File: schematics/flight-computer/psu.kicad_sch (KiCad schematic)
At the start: 32 parts, among them Q1 Si9933CDY, Q2 BSS138, U10 LTC4002-ES8, U11 MAX604, U12 MAX604, U9 BQ29200

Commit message: Rename to Lychee
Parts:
- C31, C32, C33, C34, C35, C36, C37, C38, C39, C40, C41, C42: footprint Strix:C_0402 -> Lychee:C_0402
- D15, D16: footprint Strix:B330 -> Lychee:B330
- L8: footprint Strix:L_Wuerth_HCI-7050 -> Lychee:L_Wuerth_HCI-7050
- Q1: footprint Strix:Si9933CDY -> Lychee:Si9933CDY
- Q2: footprint Strix:BSS138 -> Lychee:BSS138
- R11, R12, R13, R14, R15, R16, R17, R18, R19, R20, R21: footprint Strix:R_0402 -> Lychee:R_0402
- U10: footprint Strix:LTC4002-ES8 -> Lychee:LTC4002-ES8
- U11, U12: footprint Strix:MAX604 -> Lychee:MAX604
- U9: footprint Strix:BQ29200 -> Lychee:BQ29200
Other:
- company: (none) -> Cambridge University Spaceflight
- title: (none) -> Lychee Flight Computer
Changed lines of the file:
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@@
 (kicad_sch (version 20211123) (generator eeschema)
   (paper "A4")
+  (title_block
+    (title "Lychee Flight Computer")
+    (date "2021-12-31")
+    (rev "1")
+    (company "Cambridge University Spaceflight")
+    (comment 1 "Drawn By H. Franks")
+  )
   (junction (at 45.72 171.45) (diameter 0) (color 0 0 0 0)
   )
@@
       (effects (font (size 1.27 1.27)) (justify left))
     )
-    (property "Footprint" "Strix:C_0402" (id 2) (at 115.57 161.29 0)
+    (property "Footprint" "Lychee:C_0402" (id 2) (at 115.57 161.29 0)
       (effects (font (size 1.27 1.27)) hide)
     )
@@
       (effects (font (size 1.27 1.27)) (justify left))
     )
-    (property "Footprint" "Strix:C_0402" (id 2) (at 102.87 62.23 0)
+    (property "Footprint" "Lychee:C_0402" (id 2) (at 102.87 62.23 0)
       (effects (font (size 1.27 1.27)) hide)
     )
@@
     (property "Reference" "R13" (id 0) (at 45.72 63.5 0))
     (property "Value" "261" (id 1) (at 45.72 66.04 0))
-    (property "Footprint" "Strix:R_0402" (id 2) (at 44.45 64.77 0)
+    (property "Footprint" "Lychee:R_0402" (id 2) (at 44.45 64.77 0)
       (effects (font (size 1.27 1.27)) hide)
     )
@@
       (effects (font (size 1.27 1.27)) (justify right))
     )
-    (property "Footprint" "Strix:LTC4002-ES8" (id 2) (at 83.82 120.65 0)
+    (property "Footprint" "Lychee:LTC4002-ES8" (id 2) (at 83.82 120.65 0)
       (effects (font (size 1.27 1.27)) hide)
     )
@@
     (property "Reference" "Q1" (id 0) (at 107.95 114.3 90))
     (property "Value" "Si9933CDY" (id 1) (at 107.95 116.84 90))
-    (property "Footprint" "Strix:Si9933CDY" (id 2) (at 106.045 118.11 0)
+    (property "Footprint" "Lychee:Si9933CDY" (id 2) (at 106.045 118.11 0)
       (effects (font (size 1.27 1.27) italic) (justify left) hide)
     )
@@
       (effects (font (size 1.27 1.27)) (justify left))
     )
-    (property "Footprint" "Strix:C_0402" (id 2) (at 245.11 58.42 0)
+    (property "Footprint" "Lychee:C_0402" (id 2) (at 245.11 58.42 0)
       (effects (font (size 1.27 1.27)) hide)
     )
@@
       (effects (font (size 1.27 1.27)) (justify left))
     )
-    (property "Footprint" "Strix:C_0402" (id 2) (at 50.8 67.31 0)
+    (property "Footprint" "Lychee:C_0402" (id 2) (at 50.8 67.31 0)
       (effects (font (size 1.27 1.27)) hide)
     )
@@
     (property "Reference" "R16" (id 0) (at 49.53 158.75 0))
     (property "Value" "100" (id 1) (at 49.53 161.29 0))
-    (property "Footprint" "Strix:R_0402" (id 2) (at 48.26 163.83 0)
+    (property "Footprint" "Lychee:R_0402" (id 2) (at 48.26 163.83 0)
       (effects (font (size 1.27 1.27)) hide)
     )
@@
       (effects (font (size 1.27 1.27)) (justify left))
     )
-    (property "Footprint" "Strix:R_0402" (id 2) (at 233.68 88.9 0)
+    (property "Footprint" "Lychee:R_0402" (id 2) (at 233.68 88.9 0)
       (effects (font (size 1.27 1.27)) hide)
     )
@@
       (effects (font (size 1.27 1.27)) (justify left))
     )
-    (property "Footprint" "Strix:L_Wuerth_HCI-7050" (id 2) (at 115.57 130.81 0)
+    (property "Footprint" "Lychee:L_Wuerth_HCI-7050" (id 2) (at 115.57 130.81 0)
       (effects (font (size 1.27 1.27)) hide)
     )
@@
     (property "Reference" "D15" (id 0) (at 50.8 102.87 0))
     (property "Value" "B330" (id 1) (at 50.8 105.41 0))
-    (property "Footprint" "Strix:B330" (id 2) (at 53.34 108.712 0)
+    (property "Footprint" "Lychee:B330" (id 2) (at 53.34 108.712 0)
       (effects (font (size 1.27 1.27)) hide)
     )
@@
       (effects (font (size 1.27 1.27)) (justify left))
     )
-    (property "Footprint" "Strix:C_0402" (id 2) (at 245.11 88.9 0)
+    (property "Footprint" "Lychee:C_0402" (id 2) (at 245.11 88.9 0)
       (effects (font (size 1.27 1.27)) hide)
     )
@@
       (effects (font (size 1.27 1.27)) (justify left))
     )
-    (property "Footprint" "Strix:C_0402" (id 2) (at 83.82 160.02 0)
+    (property "Footprint" "Lychee:C_0402" (id 2) (at 83.82 160.02 0)
       (effects (font (size 1.27 1.27)) hide)
     )
@@
       (effects (font (size 1.27 1.27)) (justify left))
     )
-    (property "Footprint" "Strix:C_0402" (id 2) (at 50.8 59.69 0)
+    (property "Footprint" "Lychee:C_0402" (id 2) (at 50.8 59.69 0)
       (effects (font (size 1.27 1.27)) hide)
     )
@@
       (effects (font (size 1.27 1.27)) (justify left))
     )
-    (property "Footprint" "Strix:C_0402" (id 2) (at 63.5 73.66 0)
+    (property "Footprint" "Lychee:C_0402" (id 2) (at 63.5 73.66 0)
       (effects (font (size 1.27 1.27)) hide)
     )
@@
     (property "Reference" "R14" (id 0) (at 45.72 71.12 0))
     (property "Value" "100" (id 1) (at 45.72 73.66 0))
-    (property "Footprint" "Strix:R_0402" (id 2) (at 44.45 72.39 0)
+    (property "Footprint" "Lychee:R_0402" (id 2) (at 44.45 72.39 0)
       (effects (font (size 1.27 1.27)) hide)
     )
@@
       (effects (font (size 1.27 1.27)) (justify left top))
     )
-    (property "Footprint" "Strix:C_0402" (id 2) (at 68.58 123.19 0)
+    (property "Footprint" "Lychee:C_0402" (id 2) (at 68.58 123.19 0)
       (effects (font (size 1.27 1.27)) hide)
     )
@@
       (effects (font (size 1.27 1.27)) (justify left))
     )
-    (property "Footprint" "Strix:R_0402" (id 2) (at 102.87 48.26 0)
+    (property "Footprint" "Lychee:R_0402" (id 2) (at 102.87 48.26 0)
       (effects (font (size 1.27 1.27)) hide)
     )
@@
       (effects (font (size 1.27 1.27)) (justify left))
     )
-    (property "Footprint" "Strix:R_0402" (id 2) (at 115.57 144.78 0)
+    (property "Footprint" "Lychee:R_0402" (id 2) (at 115.57 144.78 0)
       (effects (font (size 1.27 1.27)) hide)
     )
@@
       (effects (font (size 1.27 1.27)) (justify left))
     )
-    (property "Footprint" "Strix:C_0402" (id 2) (at 201.93 58.42 0)
+    (property "Footprint" "Lychee:C_0402" (id 2) (at 201.93 58.42 0)
       (effects (font (size 1.27 1.27)) hide)
     )
@@
       (effects (font (size 1.27 1.27)) (justify left))
     )
-    (property "Footprint" "Strix:BSS138" (id 2) (at 63.5 165.735 0)
+    (property "Footprint" "Lychee:BSS138" (id 2) (at 63.5 165.735 0)
       (effects (font (size 1.27 1.27) italic) (justify left) hide)
     )
@@
       (effects (font (size 1.27 1.27)) (justify left))
     )
-    (property "Footprint" "Strix:C_0402" (id 2) (at 100.33 123.19 0)
+    (property "Footprint" "Lychee:C_0402" (id 2) (at 100.33 123.19 0)
       (effects (font (size 1.27 1.27)) hide)
     )
@@
     (property "Reference" "R12" (id 0) (at 45.72 55.88 0))
     (property "Value" "160" (id 1) (at 45.72 58.42 0))
-    (property "Footprint" "Strix:R_0402" (id 2) (at 44.45 57.15 0)
+    (property "Footprint" "Lychee:R_0402" (id 2) (at 44.45 57.15 0)
       (effects (font (size 1.27 1.27)) hide)
     )
@@
     (property "Reference" "U11" (id 0) (at 220.98 45.9232 0))
     (property "Value" "MAX604" (id 1) (at 220.98 48.2346 0))
-    (property "Footprint" "Strix:MAX604" (id 2) (at 220.98 46.355 0)
+    (property "Footprint" "Lychee:MAX604" (id 2) (at 220.98 46.355 0)
       (effects (font (size 1.27 1.27) italic) hide)
     )
@@
       (effects (font (size 1.27 1.27)) (justify right))
     )
-    (property "Footprint" "Strix:R_0402" (id 2) (at 41.91 129.54 0)
+    (property "Footprint" "Lychee:R_0402" (id 2) (at 41.91 129.54 0)
       (effects (font (size 1.27 1.27)) hide)
     )
@@
     (property "Reference" "R21" (id 0) (at 240.03 83.82 0))
     (property "Value" "100k" (id 1) (at 240.03 86.36 0))
-    (property "Footprint" "Strix:R_0402" (id 2) (at 238.76 85.09 0)
+    (property "Footprint" "Lychee:R_0402" (id 2) (at 238.76 85.09 0)
       (effects (font (size 1.27 1.27)) hide)
     )
@@
       (effects (font (size 1.27 1.27)) (justify right))
     )
-    (property "Footprint" "Strix:B330" (id 2) (at 125.222 137.16 0)
+    (property "Footprint" "Lychee:B330" (id 2) (at 125.222 137.16 0)
       (effects (font (size 1.27 1.27)) hide)
     )
@@
       (effects (font (size 1.27 1.27)) (justify left))
     )
-    (property "Footprint" "Strix:C_0402" (id 2) (at 201.93 88.9 0)
+    (property "Footprint" "Lychee:C_0402" (id 2) (at 201.93 88.9 0)
       (effects (font (size 1.27 1.27)) hide)
     )
@@
     (property "Reference" "Q1" (id 0) (at 50.8 114.3 90))
     (property "Value" "Si9933CDY" (id 1) (at 50.8 116.84 90))
-    (property "Footprint" "Strix:Si9933CDY" (id 2) (at 52.705 118.11 0)
+    (property "Footprint" "Lychee:Si9933CDY" (id 2) (at 52.705 118.11 0)
       (effects (font (size 1.27 1.27) italic) (justify left) hide)
     )
@@
       (effects (font (size 1.27 1.27)) (justify left))
     )
-    (property "Footprint" "Strix:R_0402" (id 2) (at 45.72 166.37 0)
+    (property "Footprint" "Lychee:R_0402" (id 2) (at 45.72 166.37 0)
       (effects (font (size 1.27 1.27)) hide)
     )
@@
       (effects (font (size 1.27 1.27)) (justify right))
     )
-    (property "Footprint" "Strix:BQ29200" (id 2) (at 63.5 49.53 0)
+    (property "Footprint" "Lychee:BQ29200" (id 2) (at 63.5 49.53 0)
       (effects (font (size 1.27 1.27)) hide)
     )
@@
       (effects (font (size 1.27 1.27)) (justify left))
     )
-    (property "Footprint" "Strix:R_0402" (id 2) (at 83.82 166.37 0)
+    (property "Footprint" "Lychee:R_0402" (id 2) (at 83.82 166.37 0)
       (effects (font (size 1.27 1.27)) hide)
     )
@@
     (property "Reference" "U12" (id 0) (at 220.98 76.4032 0))
     (property "Value" "MAX604" (id 1) (at 220.98 78.7146 0))
-    (property "Footprint" "Strix:MAX604" (id 2) (at 220.98 76.835 0)
+    (property "Footprint" "Lychee:MAX604" (id 2) (at 220.98 76.835 0)
       (effects (font (size 1.27 1.27) italic) hide)
     )

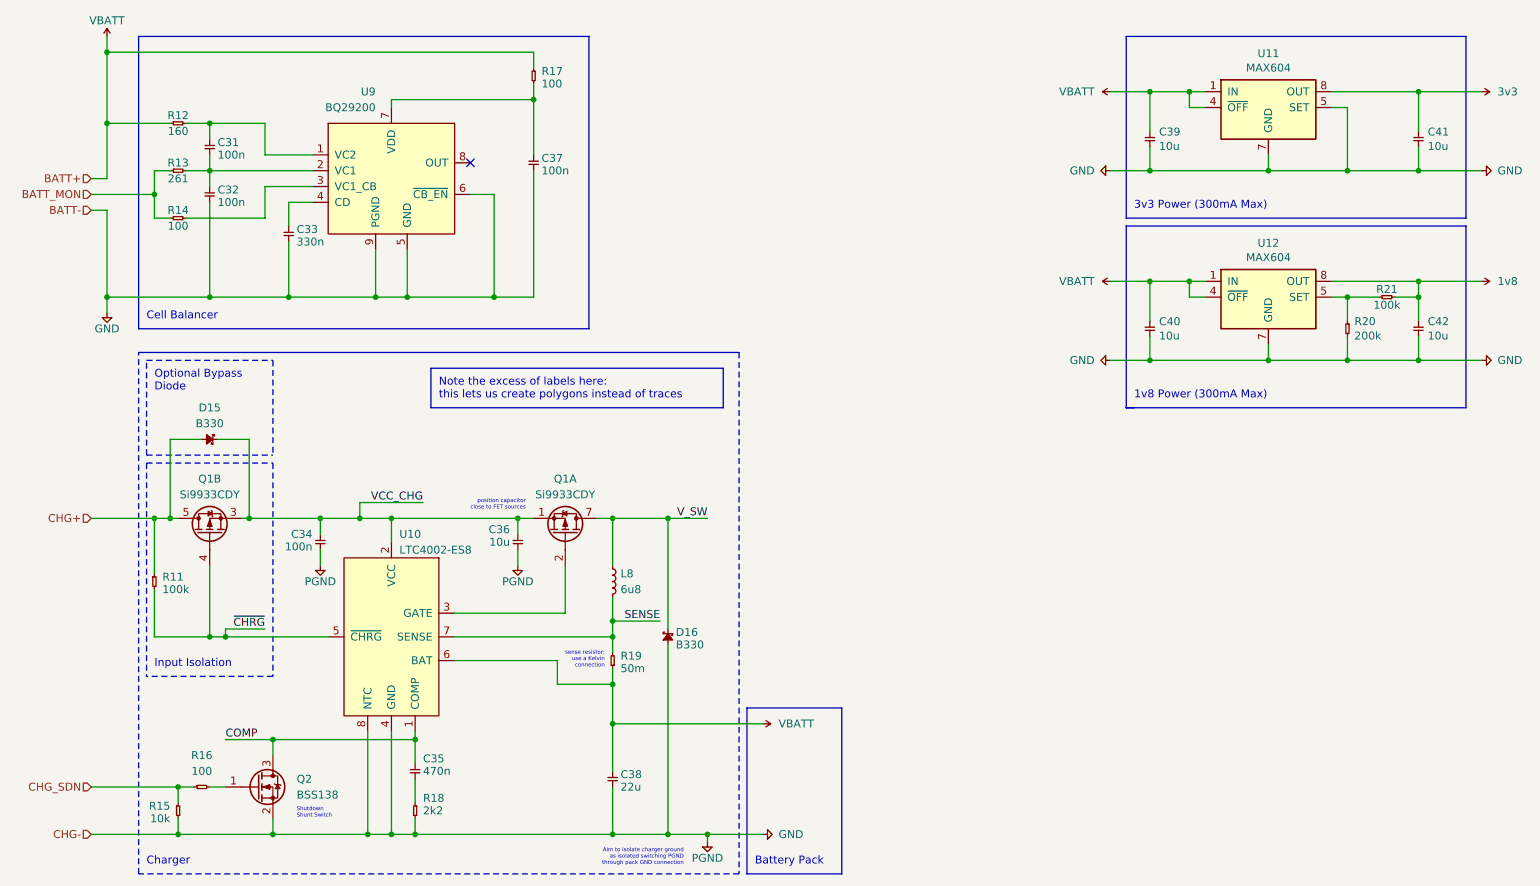
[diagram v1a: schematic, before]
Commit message: Migrate to common Strix lib via submodule
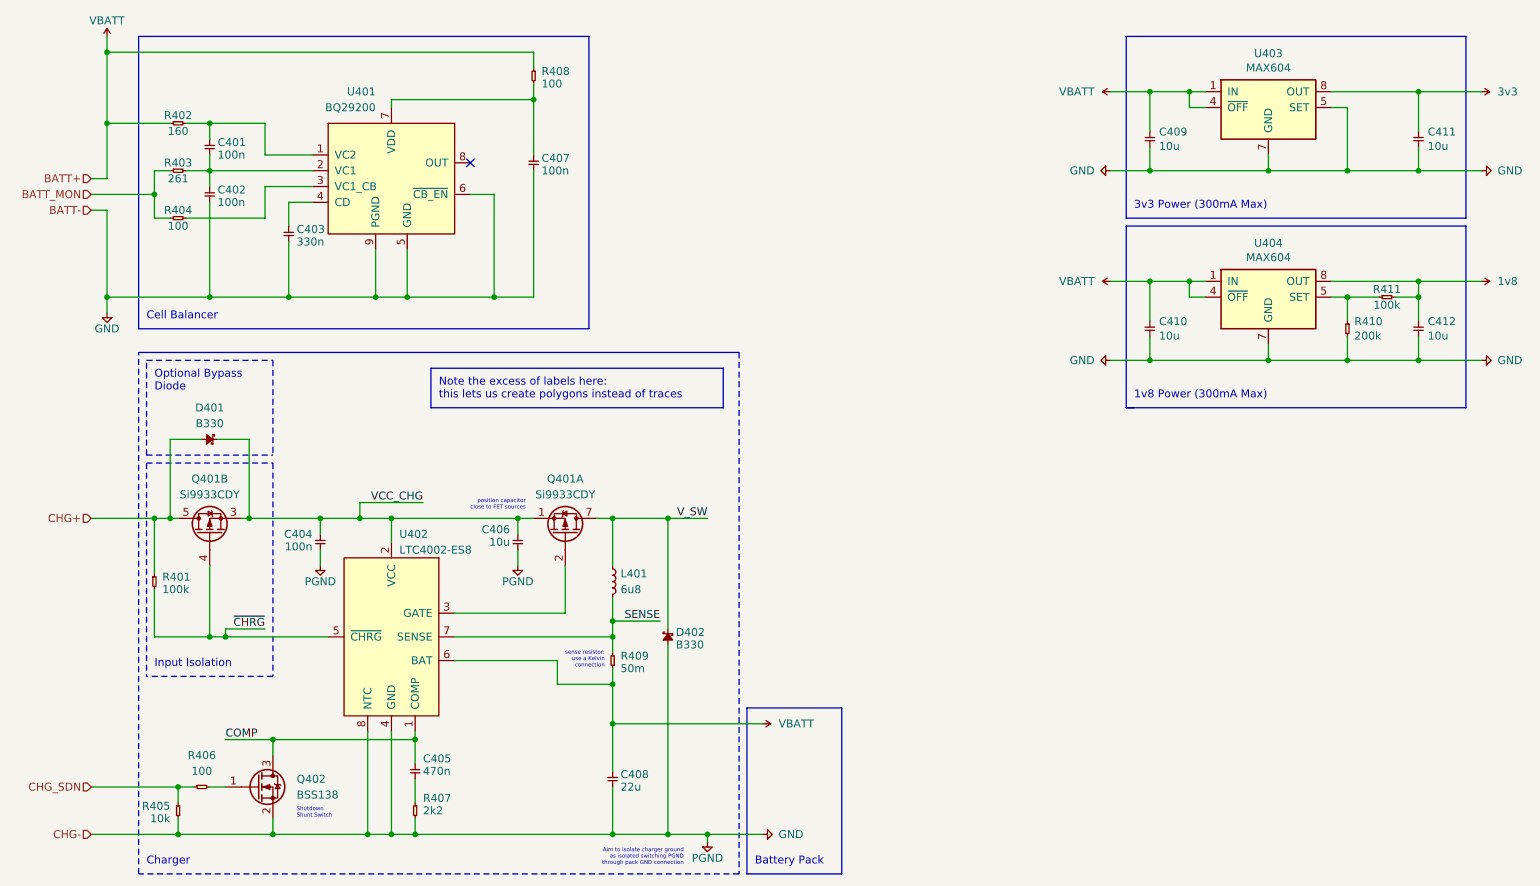
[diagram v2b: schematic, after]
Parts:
- C401: renamed from C31; footprint Lychee:C_0402 -> Strix:C_0402
- C402: renamed from C32; footprint Lychee:C_0402 -> Strix:C_0402
- C403: renamed from C33; footprint Lychee:C_0402 -> Strix:C_0402
- C404: renamed from C34; footprint Lychee:C_0402 -> Strix:C_0402
- C405: renamed from C35; footprint Lychee:C_0402 -> Strix:C_0402
- C406: renamed from C36; footprint Lychee:C_0402 -> Strix:C_0402
- C407: renamed from C37; footprint Lychee:C_0402 -> Strix:C_0402
- C408: renamed from C38; footprint Lychee:C_0402 -> Strix:C_0402
- C409: renamed from C39; footprint Lychee:C_0402 -> Strix:C_0402
- C410: renamed from C40; footprint Lychee:C_0402 -> Strix:C_0402
- C411: renamed from C41; footprint Lychee:C_0402 -> Strix:C_0402
- C412: renamed from C42; footprint Lychee:C_0402 -> Strix:C_0402
- D401: renamed from D15; footprint Lychee:B330 -> Strix:B330
- D402: renamed from D16; footprint Lychee:B330 -> Strix:B330
- L401: renamed from L8; footprint Lychee:L_Wuerth_HCI-7050 -> Strix:L_Wuerth_HCI-7050
- Q401: renamed from Q1; footprint Lychee:Si9933CDY -> Strix:Si9933CDY
- Q402: renamed from Q2; footprint Lychee:BSS138 -> Strix:BSS138
- R401: renamed from R11; footprint Lychee:R_0402 -> Strix:R_0402
- R402: renamed from R12; footprint Lychee:R_0402 -> Strix:R_0402
- R403: renamed from R13; footprint Lychee:R_0402 -> Strix:R_0402
- R404: renamed from R14; footprint Lychee:R_0402 -> Strix:R_0402
- R405: renamed from R15; footprint Lychee:R_0402 -> Strix:R_0402
- R406: renamed from R16; footprint Lychee:R_0402 -> Strix:R_0402
- R407: renamed from R18; footprint Lychee:R_0402 -> Strix:R_0402
- R408: renamed from R17; footprint Lychee:R_0402 -> Strix:R_0402
- R409: renamed from R19; footprint Lychee:R_0402 -> Strix:R_0402
- R410: renamed from R20; footprint Lychee:R_0402 -> Strix:R_0402
- R411: renamed from R21; footprint Lychee:R_0402 -> Strix:R_0402
- U401: renamed from U9; footprint Lychee:BQ29200 -> Strix:BQ29200
- U402: renamed from U10; footprint Lychee:LTC4002-ES8 -> Strix:LTC4002-ES8
- U403: renamed from U11; footprint Lychee:MAX604 -> Strix:MAX604
- U404: renamed from U12; footprint Lychee:MAX604 -> Strix:MAX604

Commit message: Update layout and models
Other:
- moved on the sheet: L401
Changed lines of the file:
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@@
     (stroke (width 0) (type default) (color 0 0 0 0))
   )
-  (wire (pts (xy 115.57 133.35) (xy 115.57 137.16))
+  (wire (pts (xy 115.57 132.08) (xy 115.57 137.16))
     (stroke (width 0) (type default) (color 0 0 0 0))
   )
@@
     (stroke (width 0) (type default) (color 0 0 0 0))
   )
-  (wire (pts (xy 115.57 120.65) (xy 115.57 128.27))
+  (wire (pts (xy 115.57 120.65) (xy 115.57 127))
     (stroke (width 0) (type default) (color 0 0 0 0))
   )
@@
     (pin "2")
   )
-  (symbol (lib_id "Strix:L_Large") (at 115.57 130.81 0) (unit 1)
-    (in_bom yes) (on_board yes)
-    (property "Reference" "L401" (id 0) (at 116.84 129.54 0)
-      (effects (font (size 1.27 1.27)) (justify left))
-    )
-    (property "Value" "6u8" (id 1) (at 116.84 132.08 0)
-      (effects (font (size 1.27 1.27)) (justify left))
-    )
-    (property "Footprint" "Strix:L_Wuerth_HCI-7050" (id 2) (at 115.57 130.81 0)
-      (effects (font (size 1.27 1.27)) hide)
-    )
-    (property "Datasheet" "~" (id 3) (at 115.57 130.81 0)
-      (effects (font (size 1.27 1.27)) hide)
-    )
-    (property "RS" "756-8588" (id 4) (at 115.57 130.81 90)
-      (effects (font (size 1.27 1.27)) hide)
-    )
-    (property "Farnell" "~" (id 5) (at 115.57 130.81 0)
-      (effects (font (size 1.27 1.27)) hide)
-    )
+  (symbol (lib_id "Strix:L_Large") (at 115.57 129.54 0) (unit 1)
+    (in_bom yes) (on_board yes)
+    (property "Reference" "L401" (id 0) (at 116.84 128.27 0)
+      (effects (font (size 1.27 1.27)) (justify left))
+    )
+    (property "Value" "6u8" (id 1) (at 116.84 130.81 0)
+      (effects (font (size 1.27 1.27)) (justify left))
+    )
+    (property "Footprint" "Strix:L_Wuerth_HCI-7050" (id 2) (at 115.57 129.54 0)
+      (effects (font (size 1.27 1.27)) hide)
+    )
+    (property "Datasheet" "~" (id 3) (at 115.57 129.54 0)
+      (effects (font (size 1.27 1.27)) hide)
+    )
+    (property "RS" "756-8588" (id 4) (at 115.57 129.54 90)
+      (effects (font (size 1.27 1.27)) hide)
+    )
+    (property "Farnell" "~" (id 5) (at 115.57 129.54 0)
+      (effects (font (size 1.27 1.27)) hide)
+    )

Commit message: Complete first draft
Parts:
- removed C404: 100n, Strix:C_0402, symbol Strix:C
- removed C405: 470n, Strix:C_0402, symbol Strix:C
- removed C406: 10u, Strix:C_0402, symbol Strix:C
- removed C408: 22u, Strix:C_0402, symbol Strix:C
- removed D401, D402: B330, Strix:B330, symbol Strix:B330
- removed L401: 6u8, Strix:L_Wuerth_HCI-7050, symbol Strix:L_Large
- removed Q401: Si9933CDY, Strix:Si9933CDY, symbol Strix:Si9933CDY
- removed Q402: BSS138, Strix:BSS138, symbol Strix:BSS138
- removed R401: 100k, Strix:R_0402, symbol Strix:R
- removed R405: 10k, Strix:R_0402, symbol Strix:R
- removed R406: 100, Strix:R_0402, symbol Strix:R
- removed R407: 2k2, Strix:R_0402, symbol Strix:R
- removed R409: 50m, Strix:R_0402, symbol Strix:R
- removed U402: LTC4002-ES8, Strix:LTC4002-ES8, symbol Strix:LTC4002-ES8
- added R404: 160, Strix:R_0402, symbol Strix:R
- C401: renamed from C409; Farnell (none) -> 3369188
- C402: renamed from C411; Farnell (none) -> 3369188
- C407: renamed from C410; Farnell (none) -> 3369188
- C408: renamed from C412; Farnell (none) -> 3369188
- R403: value 261 -> 100; Farnell 2303485 -> 2447552
- R406: renamed from R411; Farnell (none) -> 2447094
- R407: renamed from R410; Farnell (none) -> 2059185
- U401: renamed from U403; Farnell (none) -> 2799174
- U403: renamed from U404; Farnell (none) -> 2799174
- renumbered C401 to C403, C407 to C404, C402 to C405, C403 to C406, R408 to R401, R404 to R405, U401 to U402
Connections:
- net at C403.2, C405.1, U402.2 (VC1): now also R404.2; no longer R403.2
- new net: R403.2, R404.1
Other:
- note removed: "Aim to isolate charger ground as isolated switching PGND through pack GND connection"
- note removed: "Battery Pack"
- note removed: "Charger"
- note removed: "Input Isolation"
- note removed: "Note the excess of labels here: this lets us create polygons instead of traces"
- note removed: "Optional Bypass Diode"
- note removed: "Shutdown Shunt Switch"
- note removed: "position capacitor close to FET sources"
- note removed: "sense resistor: use a Kelvin connection"
- moved on the sheet: C403, C404, C405, C406, R401, R402, R405, U402
